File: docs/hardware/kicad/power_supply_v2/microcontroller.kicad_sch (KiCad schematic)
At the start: 1 part, among them U10 NUCLEO-G474RE

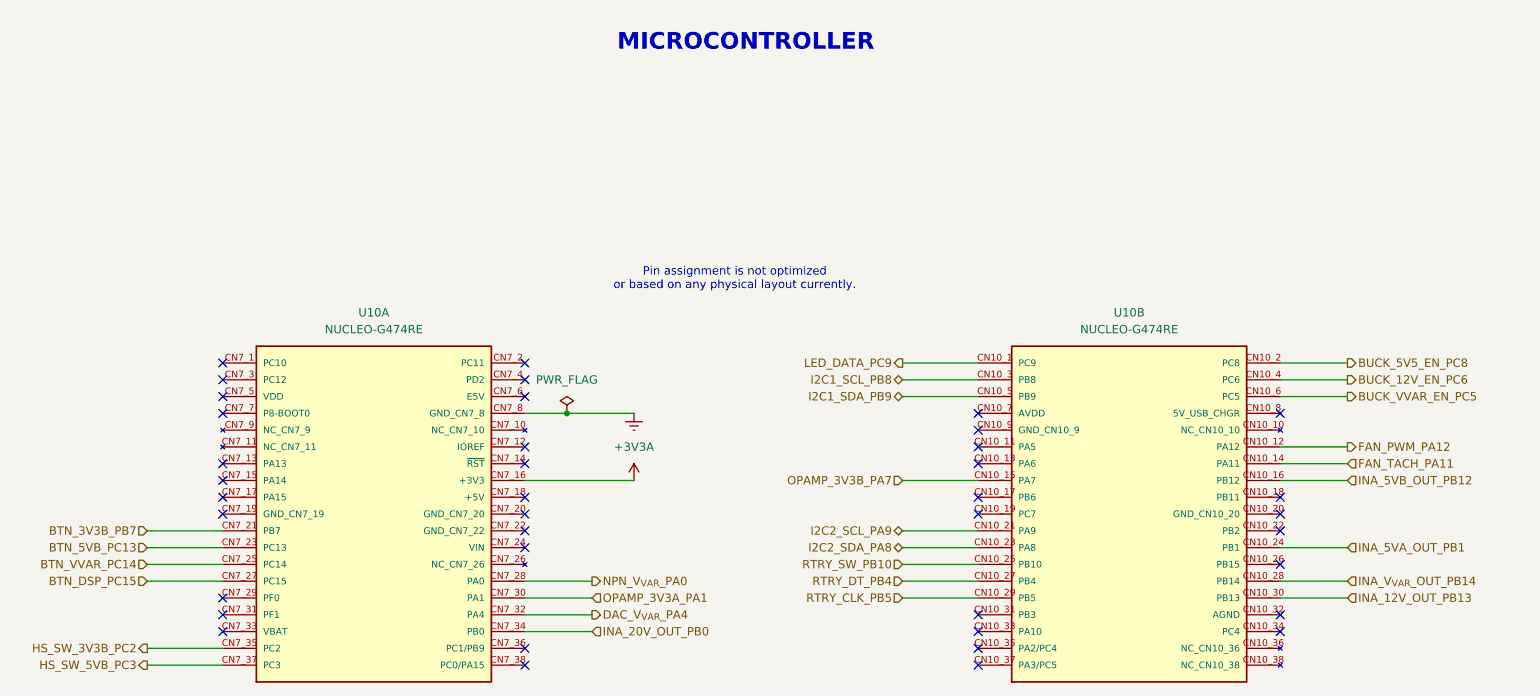
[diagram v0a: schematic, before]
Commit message: updated schematic for LC filters and added voltage injection to other… (#4)
* updated schematic for LC filters and added voltage injection to other bucks

* rework buck resistor divider values + add fb injection to 3V3 and 5V rail bucks

* remove redundant switches for variable rail

* remove datasheets for components no longer used in rev A3

---------

Co-authored-by: chris <chris@laptop.malecki.com>
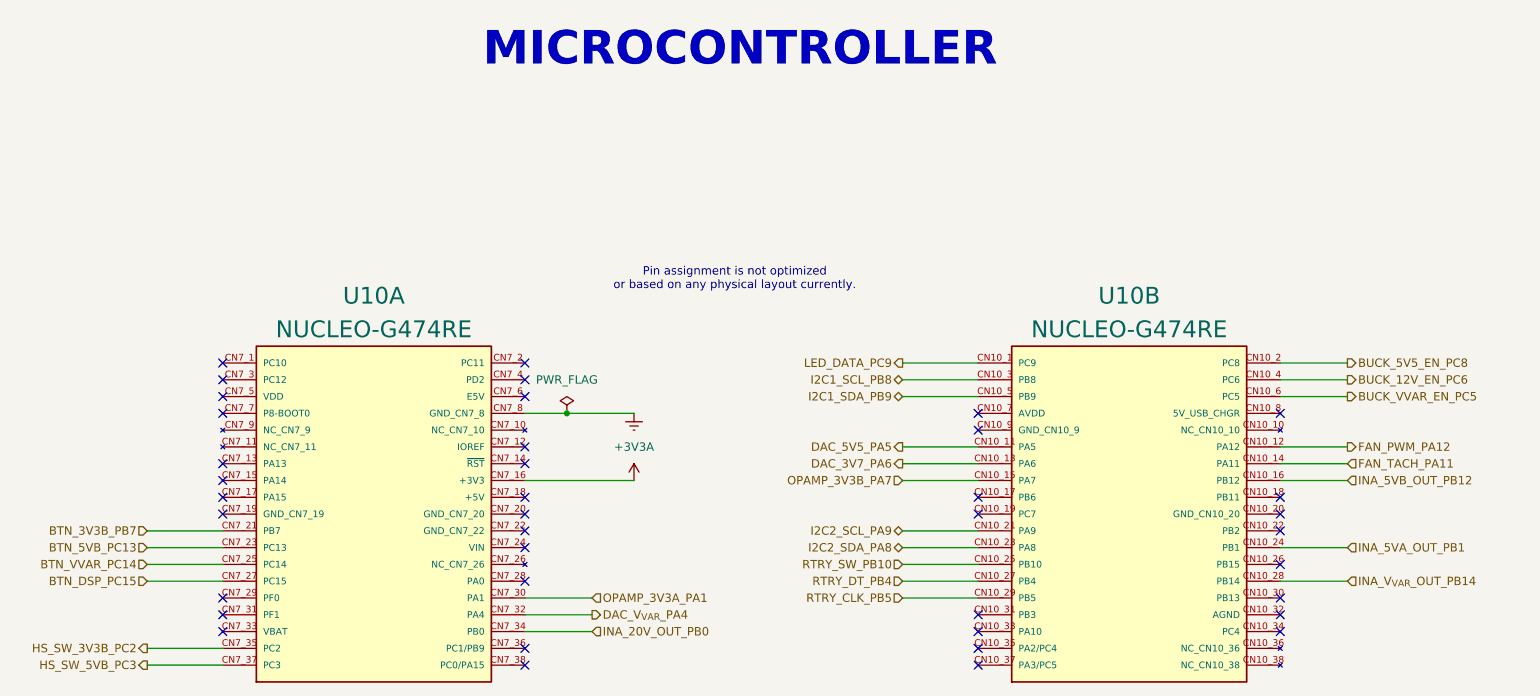
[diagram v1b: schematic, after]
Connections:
- net DAC_5V5_PA5: now reaches U10.CN10_11 (PA5)
- net DAC_3V7_PA6: now reaches U10.CN10_13 (PA6)
- net INA_12V_OUT_PB13: no longer names the net of U10.CN10_30 (PB13)
- net NPN_V_{VAR}_PA0: no longer names the net of U10.CN7_28 (PA0)
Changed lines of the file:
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@@
 	(title_block
 		(title "Digital Variable DC Bench Power Supply")
-		(date "2026-04-27")
-		(rev "1")
+		(date "2026-05-01")
+		(rev "A3")
 	)
 	(text "MICROCONTROLLER"
 		(exclude_from_sim no)
-		(at 132.08 19.05 0)
-		(effects
-			(font
-				(size 2.54 2.54)
+		(at 111.76 21.59 0)
+		(effects
+			(font
+				(size 5.08 5.08)
 				(thickness 1.016)
 				(bold yes)
@@
 	)
 	(no_connect
+		(at 232.41 101.6)
+	)
+	(no_connect
 		(at 118.11 68.58)
 	)
@@
 	)
 	(no_connect
-		(at 186.69 81.28)
-	)
-	(no_connect
 		(at 72.39 81.28)
 	)
@@
 	)
 	(no_connect
+		(at 118.11 99.06)
+	)
+	(no_connect
 		(at 118.11 81.28)
 	)
@@
 	)
 	(no_connect
-		(at 186.69 78.74)
-	)
-	(no_connect
 		(at 186.69 88.9)
 	)
@@
 	(wire
 		(pts
-			(xy 232.41 101.6) (xy 242.57 101.6)
-		)
-		(stroke
-			(width 0)
-			(type default)
-		)
-	)
-	(wire
-		(pts
 			(xy 175.26 101.6) (xy 186.69 101.6)
 		)
@@
 	(wire
 		(pts
+			(xy 175.26 78.74) (xy 186.69 78.74)
+		)
+		(stroke
+			(width 0)
+			(type default)
+		)
+	)
+	(wire
+		(pts
 			(xy 60.96 109.22) (xy 72.39 109.22)
 		)
@@
 	(wire
 		(pts
-			(xy 118.11 99.06) (xy 128.27 99.06)
+			(xy 175.26 81.28) (xy 186.69 81.28)
 		)
 		(stroke
@@
 			(width 0)
 			(type default)
+		)
+	)
+	(hierarchical_label "DAC_5V5_PA5"
+		(shape output)
+		(at 175.26 78.74 180)
+		(effects
+			(font
+				(size 1.27 1.27)
+			)
+			(justify right)
 		)
 	)
@@
 		)
 	)
-	(hierarchical_label "INA_12V_OUT_PB13"
-		(shape input)
-		(at 242.57 101.6 0)
-		(effects
-			(font
-				(size 1.27 1.27)
-			)
-			(justify left)
-		)
-	)
 	(hierarchical_label "DAC_V_{VAR}_PA4"
 		(shape output)
@@
 		)
 	)
+	(hierarchical_label "DAC_3V7_PA6"
+		(shape output)
+		(at 175.26 81.28 180)
+		(effects
+			(font
+				(size 1.27 1.27)
+			)
+			(justify right)
+		)
+	)
 	(hierarchical_label "HS_SW_5VB_PC3"
 		(shape output)
@@
 			)
 			(justify right)
-		)
-	)
-	(hierarchical_label "NPN_V_{VAR}_PA0"
-		(shape output)
-		(at 128.27 99.06 0)
-		(effects
-			(font
-				(size 1.27 1.27)
-			)
-			(justify left)
 		)
 	)
@@
 		(on_board yes)
 		(dnp no)
-		(fields_autoplaced yes)
 		(property "Reference" "U10"
-			(at 95.25 58.42 0)
-			(effects
-				(font
-					(size 1.27 1.27)
+			(at 95.25 55.88 0)
+			(effects
+				(font
+					(size 2.54 2.54)
 				)
 			)
@@
 			(effects
 				(font
-					(size 1.27 1.27)
+					(size 2.54 2.54)
 				)
 			)
@@
 		(on_board yes)
 		(dnp no)
-		(fields_autoplaced yes)
 		(property "Reference" "U10"
-			(at 209.55 58.42 0)
-			(effects
-				(font
-					(size 1.27 1.27)
+			(at 209.55 55.88 0)
+			(effects
+				(font
+					(size 2.54 2.54)
 				)
 			)
@@
 			(effects
 				(font
-					(size 1.27 1.27)
-				)
-			)
+					(size 2.54 2.54)
+				)
+			)
